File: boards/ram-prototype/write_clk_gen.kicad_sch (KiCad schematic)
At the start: 24 parts, among them U1 74LVC1G00, U2 74LVC1G00, U3 74LVC1G00, U4 74LVC1G00, U5 74LVC1G00, U6 74LVC1G00, U7 74LVC1G00, U8 74LVC1G00

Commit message: Partway through erc debugging
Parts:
- removed D1, D2, D3, D4, D5, D6, D7, D8: Red, symbol LED_Small
- removed R1, R2, R3, R4, R5, R6, R7, R8: 680R, symbol R_Small
- removed U1, U2, U3, U4, U5, U6, U7, U8: 74LVC1G00, symbol 74LVC1G00
- added D1, D2, D3, D4, D5, D6, D7, D8: Red, symbol Device:LED_Small
- added R1, R2, R3, R4, R5, R6, R7, R8: 680R, symbol Device:R_Small
- added U1, U2, U3, U4, U5, U6, U7, U8: 74LVC1G00, symbol 74xGxx:74LVC1G00
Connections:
- net GND: now also D1.1 (K), D2.1 (K), D3.1 (K), D4.1 (K), D5.1 (K), D6.1 (K), D7.1 (K), D8.1 (K), U1.3 (GND), U2.3 (GND), U3.3 (GND), U4.3 (GND), U5.3 (GND), U6.3 (GND), U7.3 (GND), U8.3 (GND)
- net SEL0: now also U1.2
- net SEL1: now also U2.2
- net SEL2: now also U3.2
- net SEL3: now also U4.2
- net SEL4: now also U5.2
- net SEL5: now also U6.2
- net SEL6: now also U7.2
- net SEL7: now also U8.2
- net VCC: now also U1.5 (VCC), U2.5 (VCC), U3.5 (VCC), U4.5 (VCC), U5.5 (VCC), U6.5 (VCC), U7.5 (VCC), U8.5 (VCC)
- net WRITE_ACTIVE: now also U1.1, U2.1, U3.1, U4.1, U5.1, U6.1, U7.1, U8.1
- net WRITE_CLK_0: now also R1.1, U1.4
- net WRITE_CLK_1: now also R2.1, U2.4
- net WRITE_CLK_2: now also R3.1, U3.4
- net WRITE_CLK_3: now also R4.1, U4.4
- net WRITE_CLK_4: now also R5.1, U5.4
- net WRITE_CLK_5: now also R6.1, U6.4
- net WRITE_CLK_6: now also R7.1, U7.4
- net WRITE_CLK_7: now also R8.1, U8.4
- new net: D7.2 (A), R7.2
- new net: D2.2 (A), R2.2
- new net: D3.2 (A), R3.2
- new net: D6.2 (A), R6.2
- new net: D1.2 (A), R1.2
- new net: D4.2 (A), R4.2
- new net: D5.2 (A), R5.2
- new net: D8.2 (A), R8.2

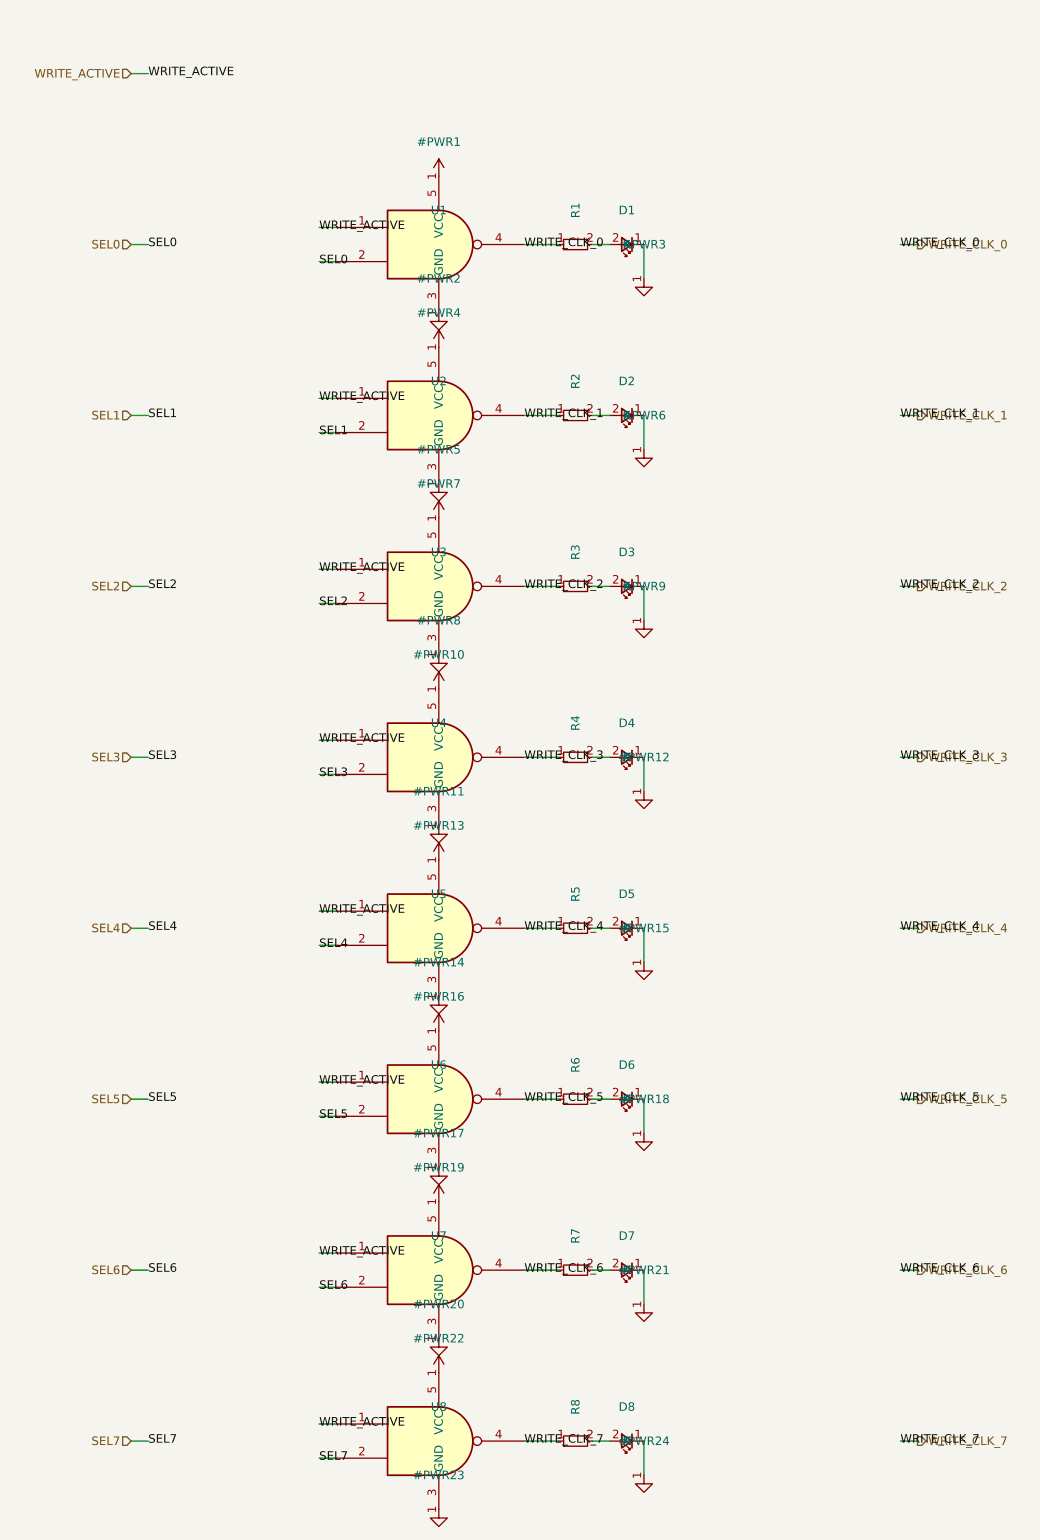
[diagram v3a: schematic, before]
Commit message: Start cleaning up the schematic
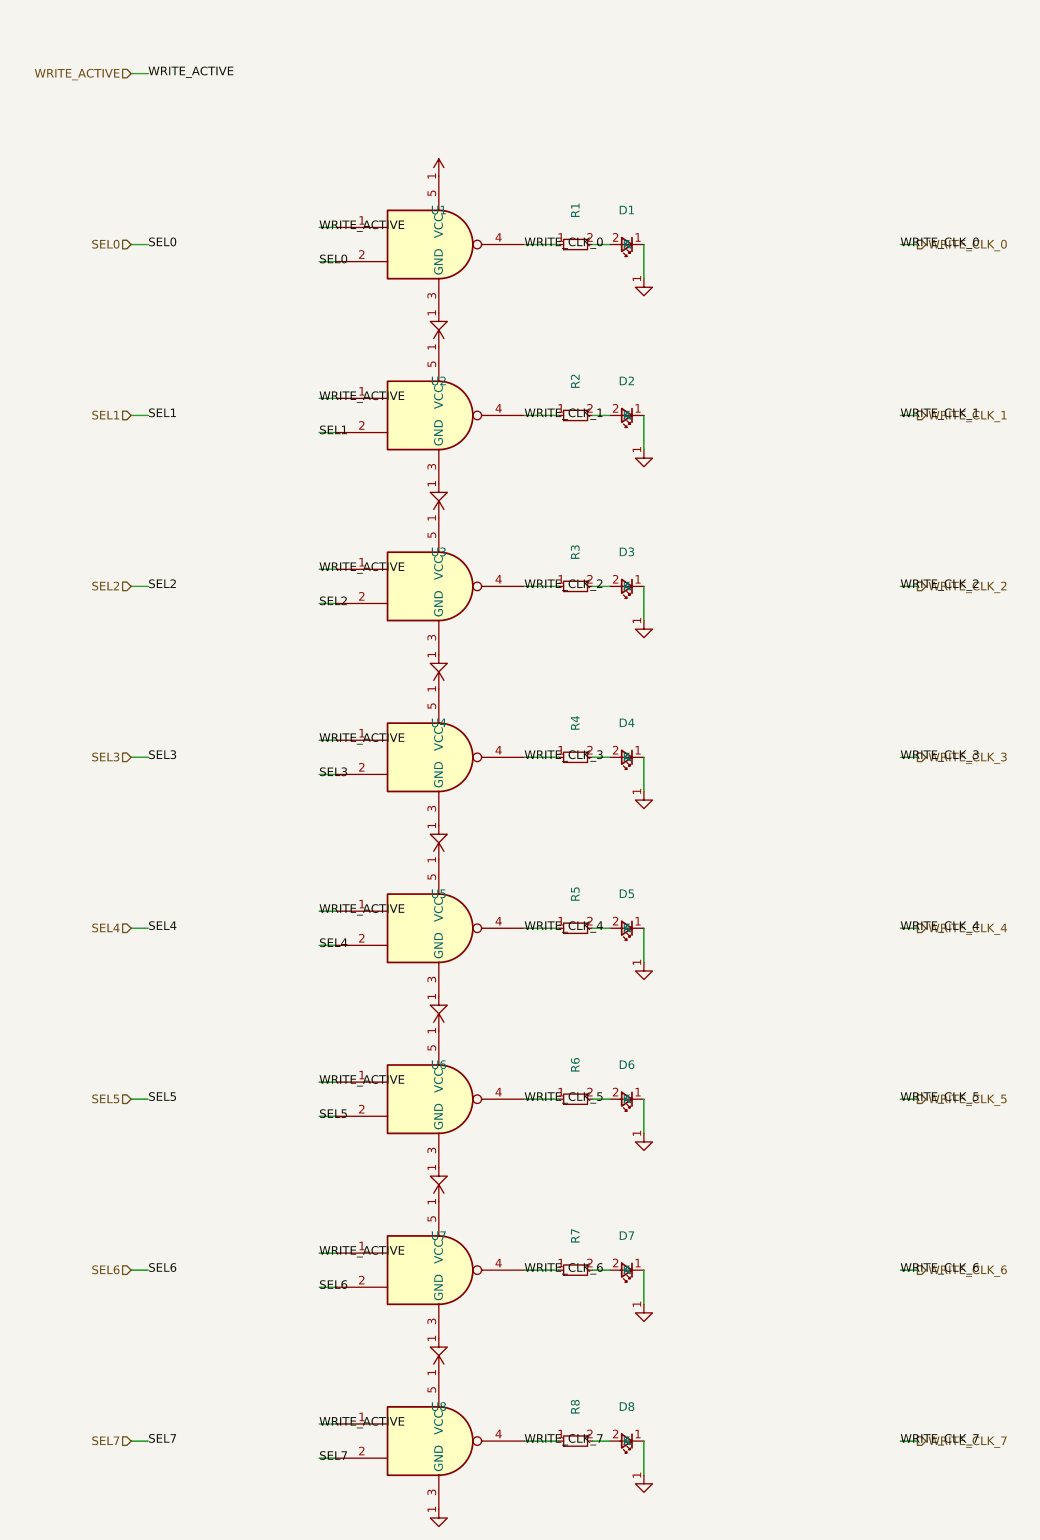
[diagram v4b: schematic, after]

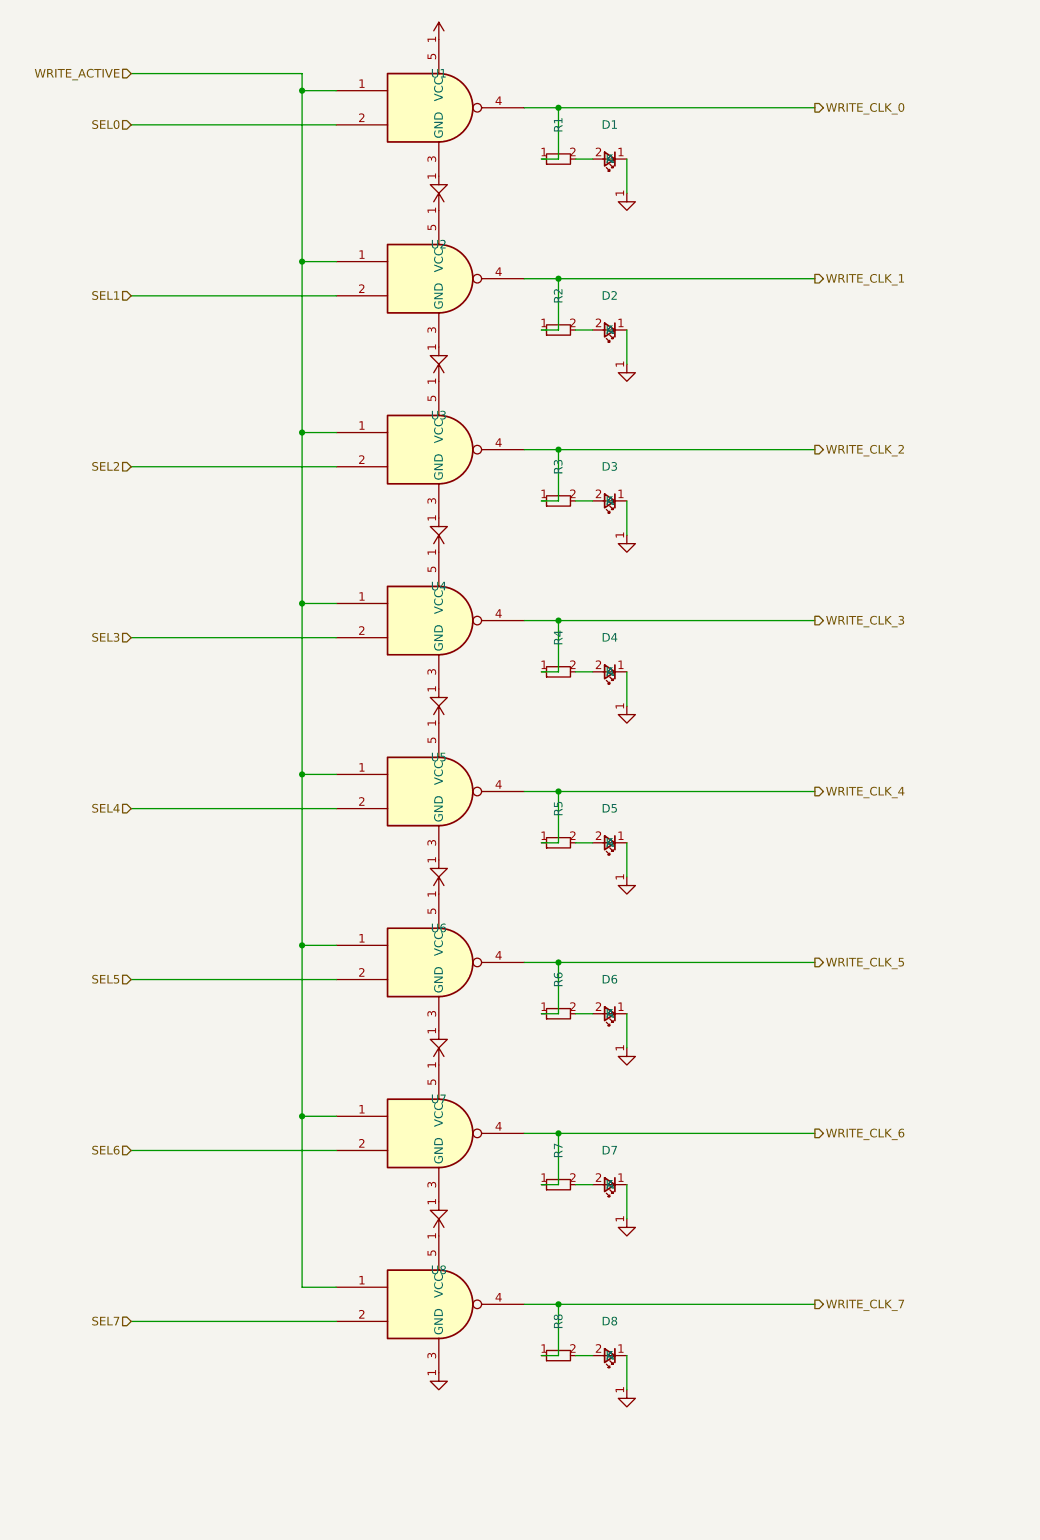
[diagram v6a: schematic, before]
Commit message: Create verification script
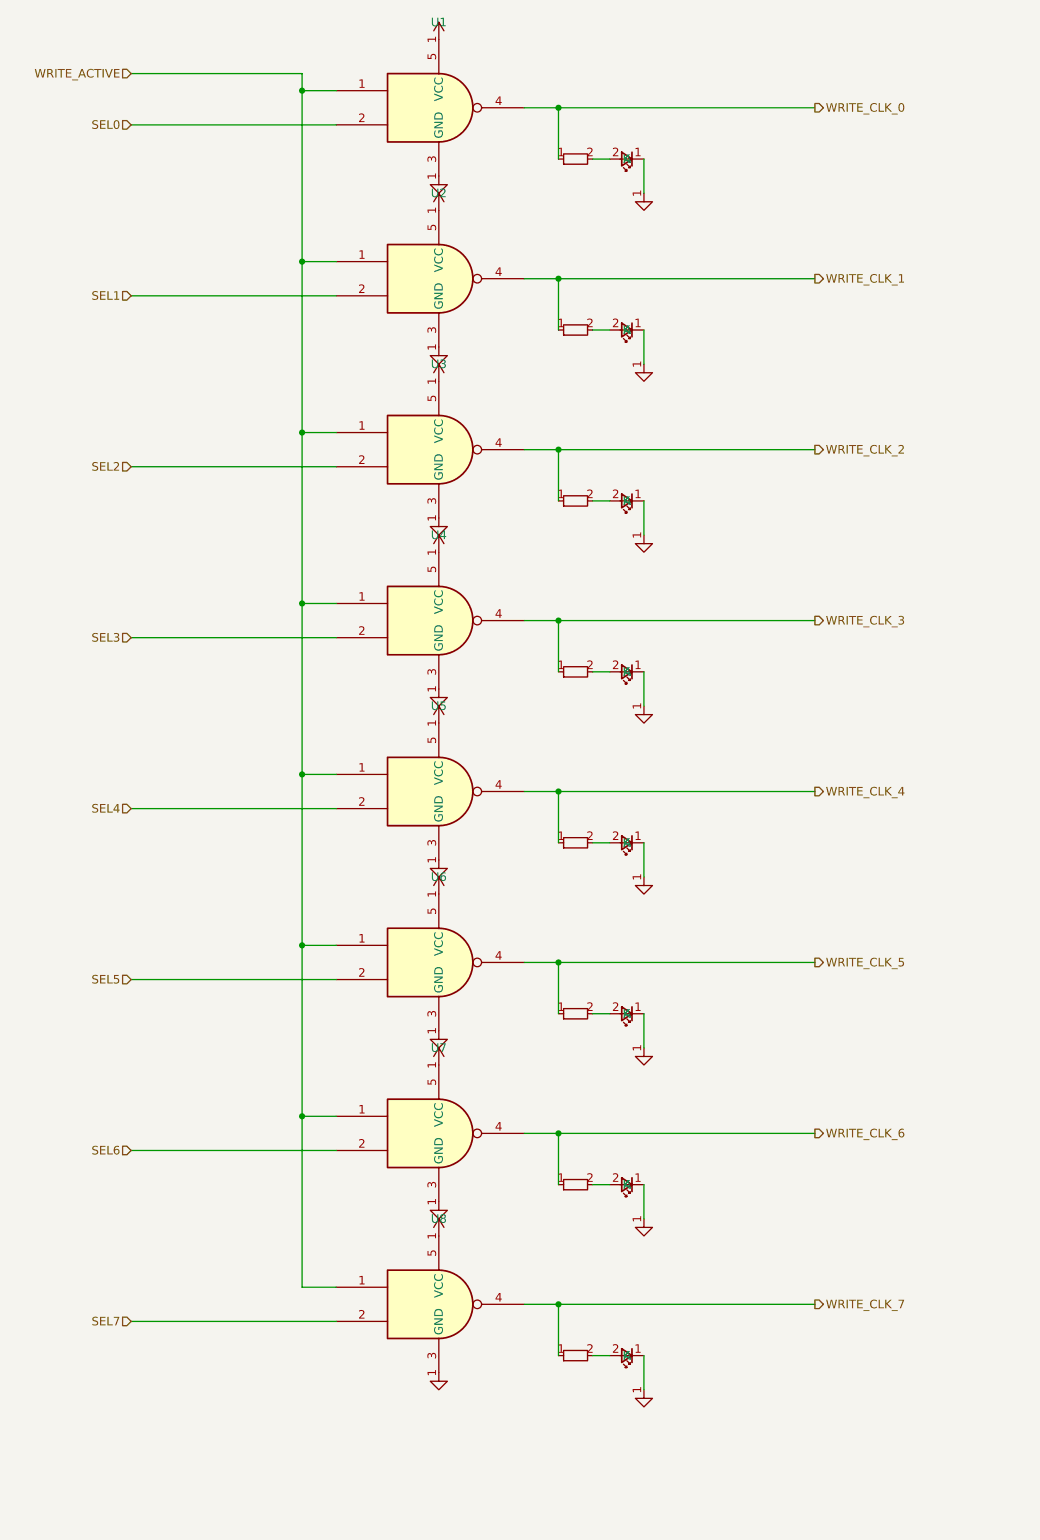
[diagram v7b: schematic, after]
